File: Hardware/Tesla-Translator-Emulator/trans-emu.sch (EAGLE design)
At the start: 40 parts, among them IC1 MIC5233-3.3YM5-TR, Q1 PMOSFET, Q2 NMOSFET, U1 STM32F413RGT6, U2 TJA1042HVSON, U3 TJA1042HVSON, U4 TJA1042HVSON, Y1 CRYSTAL-3.2X2.54-PIN

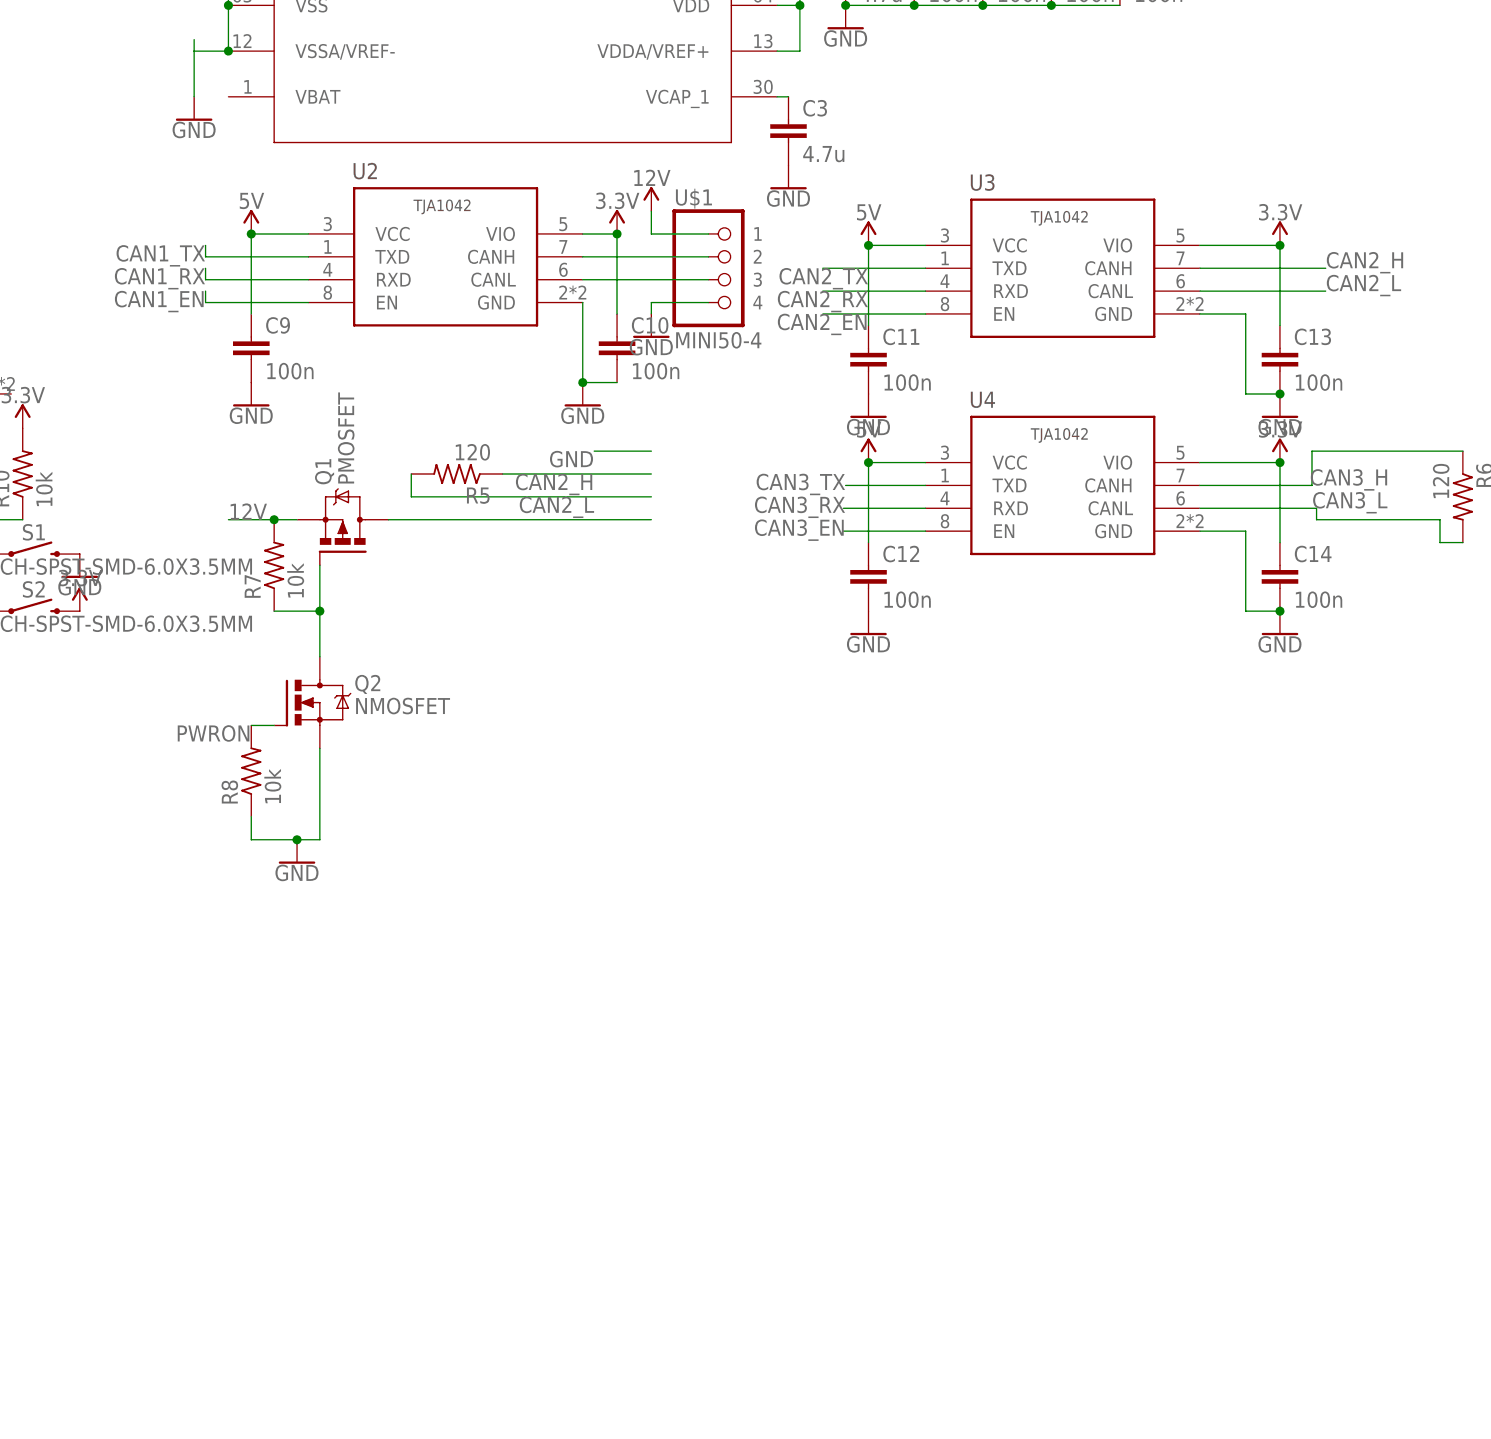
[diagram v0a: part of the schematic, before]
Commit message: Ibooster board updates
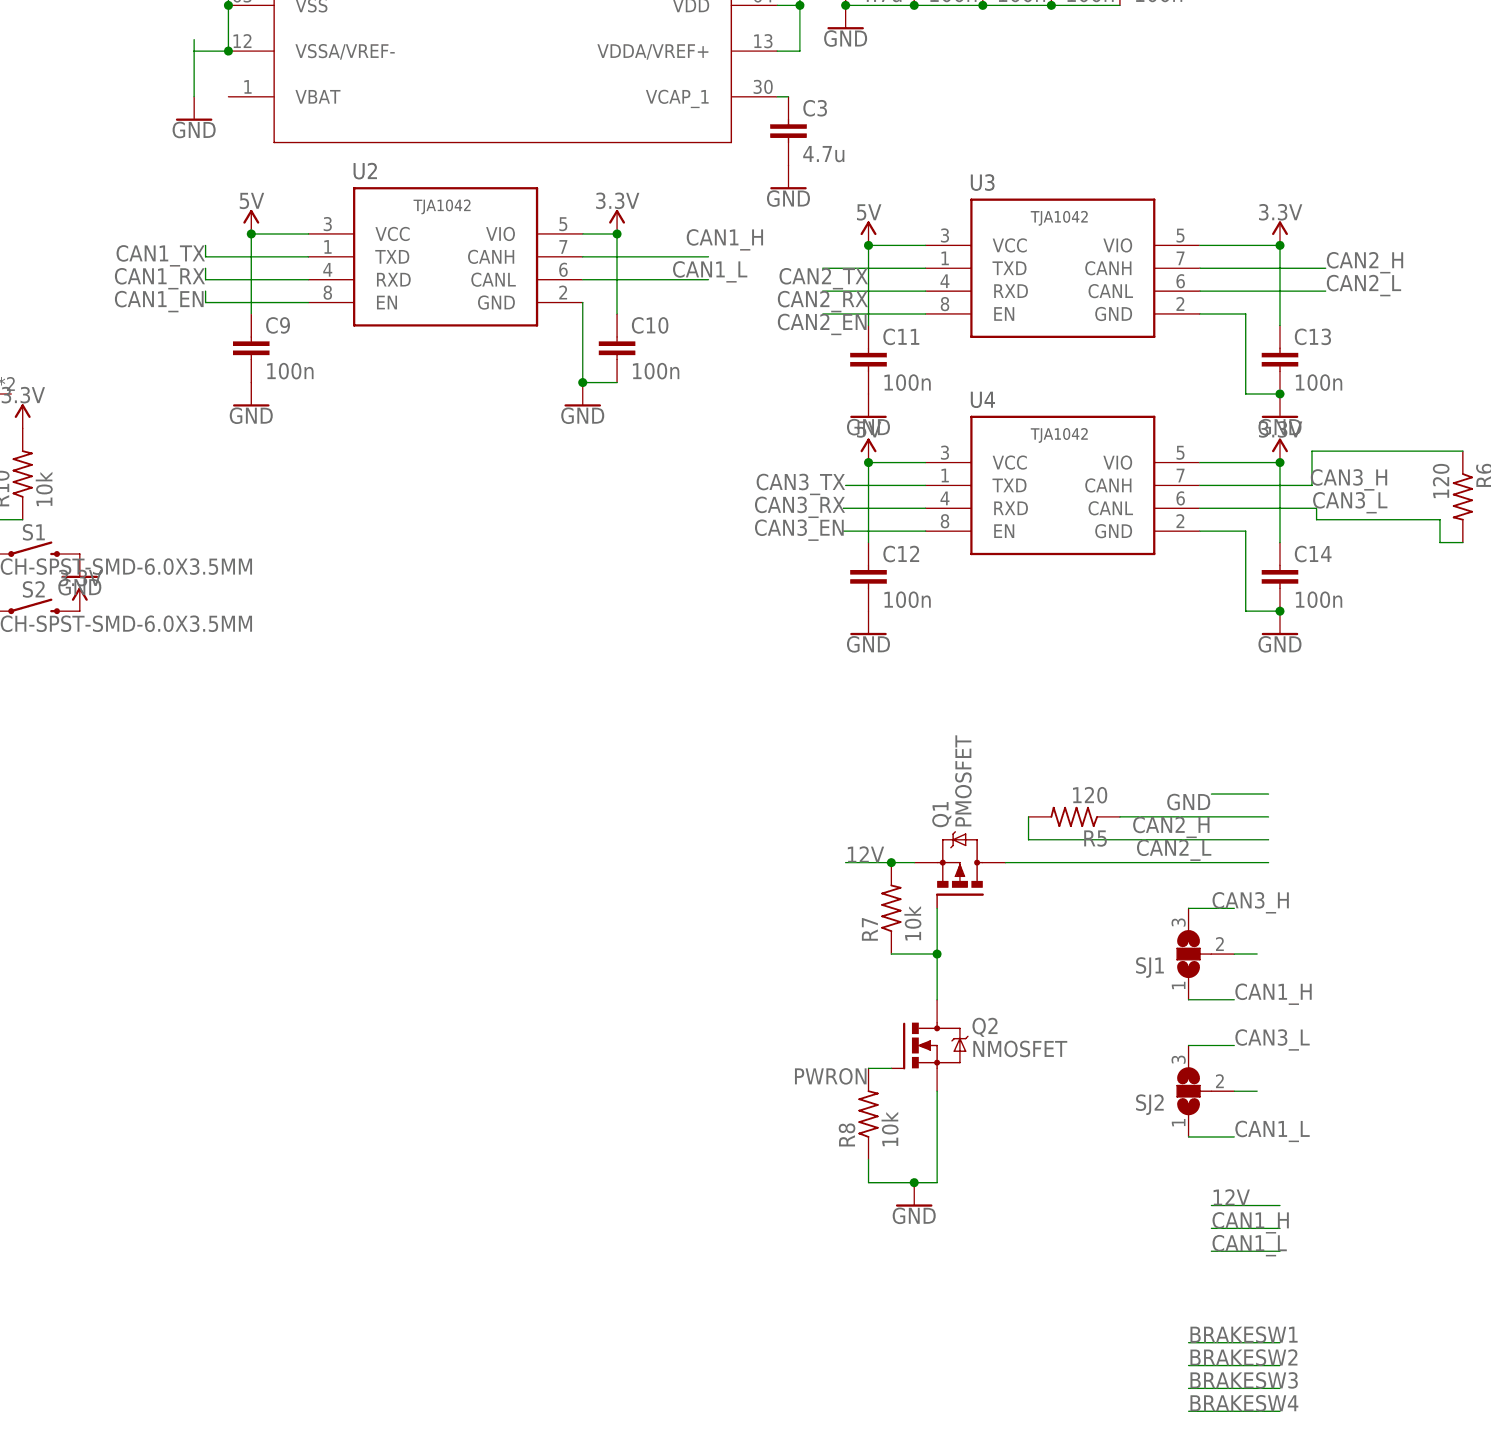
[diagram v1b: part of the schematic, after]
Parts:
- removed U$1: MINI50-4, interceptor:MINI50-4
- added SJ1, SJ2: (no value), jumper:SJ2W
- U2, U3, U4: value TJA1042HVSON -> TJA1042; device comma.ai:TJA1042HVSON -> CM,118:TJA1042
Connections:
- new net CAN1_H: SJ1.1, U2.CANH
- new net CAN1_L: SJ2.1, U2.CANL
- net 12V: no longer U$1.1
- net CAN3_H: now also SJ1.3
- net CAN3_L: now also SJ2.3
- net GND: no longer U$1.4
- net N$12: now also SJ1.2; no longer U$1.2, U2.CANH
- net N$14: now also SJ2.2; no longer U$1.3, U2.CANL
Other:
- moved on the sheet: Q1, Q2, R5, R7, R8, U2, U3, U4

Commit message: ibooster schematic and water controller
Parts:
- added J2: 64334-0100, 64334-0100:64334-0100
- added K1: V23086C2001A403, SamacSys_Parts:V23086C2001A403
- added Q3: NMOSFET, Transistor:NMOSFETSOT23
- added R11: 10k, comma.ai:R0402
- added U$1: FUSE_CHIP-1206(3216-METRIC), Circuit-Protection:FUSE_CHIP-1206(3216-METRIC)
- Q1: value PMOSFET -> 4.3A/20V/54mΩ; device Transistor:PMOSFET_SOT23 -> SparkFun-DiscreteSemi:MOSFET_PCH-IRLML2244
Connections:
- removed net N$15: Q1.D
- new net BLIGHT: Q3.G, R11.2, U1A.PB13
- new net COM1: J2.A2, K1.COM_1
- new net COM2: J2.B2, K1.COM_2
- new net IBSTIN: J2.H1, Q1.S, R7.2
- new net IBSTOUT: Q1.D, U$1.2
- new net N$17: K1.COIL_1, K1.COIL_3, Q3.D
- new net N$18: J2.G1, U$1.1
- new net NC1: J2.A1, K1.NC_1
- new net NC2: J2.B1, K1.NC_2
- new net NO1: J2.A3, K1.NO_1
- new net NO2: J2.B3, K1.NO_2
- net 12V: now also J2.C1, K1.COIL_2, K1.COIL_4; no longer Q1.S, R7.2
- net CAN1_H: now also J2.C2
- net CAN1_L: now also J2.C3
- net CAN2_H: now also J2.E2
- net CAN2_L: now also J2.E1
- net GND: now also J2.C4, J2.G2, J2.H2, Q3.S, R11.1
- net N$12: now also J2.F2
- net N$14: now also J2.F1
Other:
- moved on the sheet: Q2, R5, R7, R8, SJ1, SJ2
